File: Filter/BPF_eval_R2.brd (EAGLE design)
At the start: 35.6 x 33.3 mm, 7 parts, among them J1 142-0711-821, J2 142-0711-821, J3 142-0711-821, J4 142-0711-821, U1 885071-A

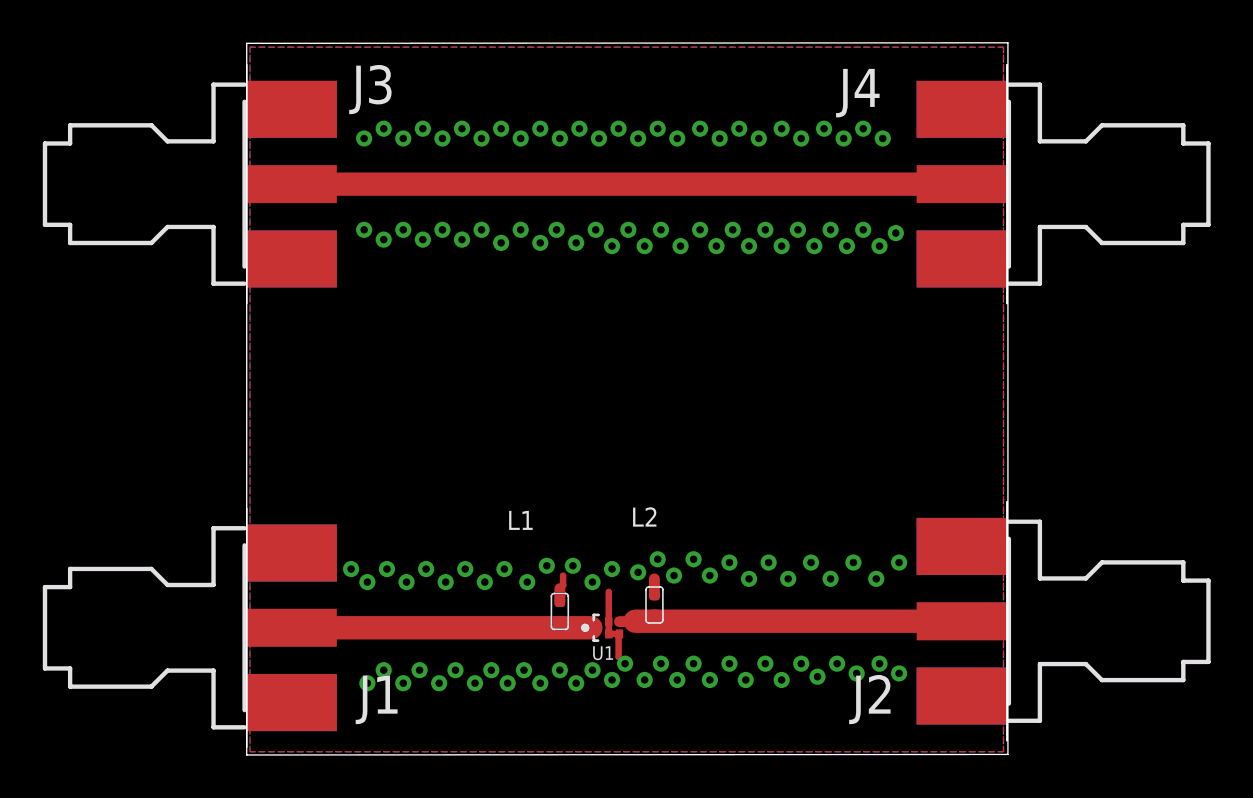
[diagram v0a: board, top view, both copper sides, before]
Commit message: Fixed Nathan's filter board. Mostly EAGLE stupidity problems. - Switched SMA connectors to the PSAS standard. - Switched grid to 10 mil because OCD. - Loaded OSH Park 2 layer DRC. - Made "RF" class to keep away the ground plane. - Fixed vias (were only layer 1-2, not 1-16). - Added text. Should be good to go?
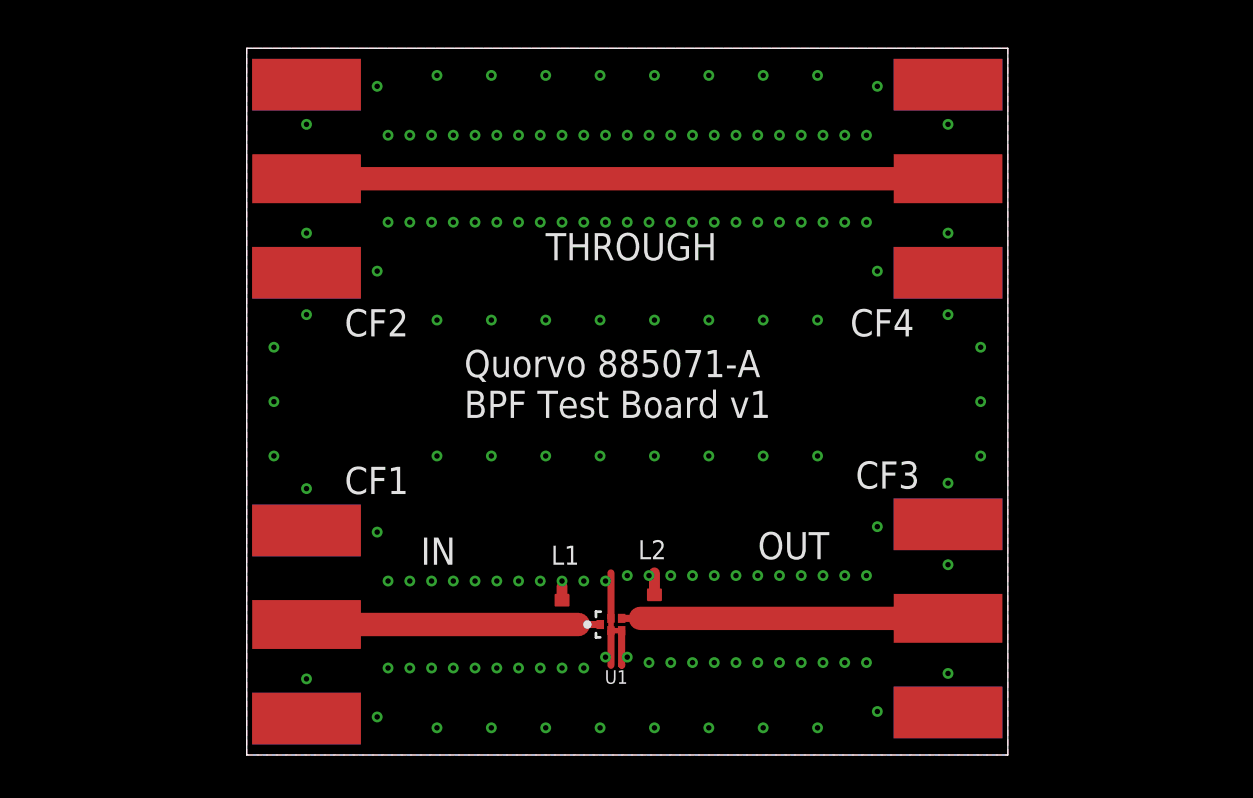
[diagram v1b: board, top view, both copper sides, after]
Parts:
- removed J1, J2, J3, J4: 142-0711-821, con-coax:J502-ND-142-0711-821/826
- added CF1, CF2, CF3, CF4: SMA-CINCH-END-FIRE, psas_c3_team05:SMAJ716-ND
- L1, L2: device Seeed-Inductor:L0402 -> rcl_custom:.0402-B-NOSILK
- moved U1 0.18 mm to (17.0, 6.10)
- moved L1 0.10 mm to (14.7, 6.73)
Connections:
- removed net N$1: J1.1, L1.1, U1.1
- removed net N$2: J2.1, L2.1, U1.4
- removed net N$3: J3.1, J4.1
- new net IN: CF1.P$3, L1.1, U1.1
- new net OUT: CF3.P$3, L2.1, U1.4
- new net THROUGH: CF2.P$3, CF4.P$3
- net GND: now also CF1.GND1, CF1.GND2, CF1.GND3, CF1.GND4, CF2.GND1, CF2.GND2, CF2.GND3, CF2.GND4, CF3.GND1, CF3.GND2, CF3.GND3, CF3.GND4, CF4.GND1, CF4.GND2, CF4.GND3, CF4.GND4; no longer J1.G@1, J1.G@2, J2.G@1, J2.G@2, J2.G@3, J3.G@1, J3.G@2, J3.G@3, J4.G@1, J4.G@2
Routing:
- net N$3: track 31.3 -> 0.00 mm
- net THROUGH: track 0.00 -> 30.0 mm
- net N$2: track 17.7 -> 0.00 mm
- net OUT: track 0.00 -> 16.1 mm
- net N$1: track 15.9 -> 0.00 mm
- net IN: track 0.00 -> 15.1 mm
- net GND: track 5.60 -> 8.11 mm, vias 117 -> 149
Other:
- board size 35.6 x 33.3 mm -> 35.6 x 33 mm
- board text added: "IN"
- board text added: "OUT"
- board text added: "Quorvo 885071-A BPF Test Board v1"
- board text added: "THROUGH"
